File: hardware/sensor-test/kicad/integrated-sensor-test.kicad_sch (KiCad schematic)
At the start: 48 parts, among them J1 TYPE-C-31-M-12, J90 USB_B_Micro, J91 Conn_02x18_Odd_Even, J92 Conn_02x18_Odd_Even, J93 Conn_01x02, U1 RP2040, U10 USBLC6-2SC6, U2 W25Q128JVS, U3 AP2112K-3.3TRG1, U90 NCP1117-3.3_SOT223, Y1 ABLS-12.000MHZ-B4-T

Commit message: Mark retired Micro-USB data pins unconnected
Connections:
- net +1V1: no longer C11.1, C12.1, C13.1, U1.23 (DVDD), U1.45 (VREG_VOUT), U1.50 (DVDD)
- net +3V3: no longer C10.1, C16.1, C17.1, C3.1, C4.1, C5.1, C6.1, C7.1, C8.1, C9.1, C91.1, J91.2 (Pin_2), R8.1, U1.1 (IOVDD), U1.10 (IOVDD), U1.22 (IOVDD), U1.33 (IOVDD), U1.42 (IOVDD), U1.43 (ADC_AVDD), U1.44 (VREG_IN), U1.48 (USB_VDD), U1.49 (IOVDD), U2.8 (VCC), U90.2 (VO)
- net GND: no longer C10.2, C11.2, C12.2, C13.2, C15.2, C16.2, C3.2, C4.2, C5.2, C6.2, C7.2, C8.2, C9.2, J90.5 (GND), J90.6 (Shield), J91.1 (Pin_1), J91.11 (Pin_11), J91.13 (Pin_13), J91.15 (Pin_15), J91.17 (Pin_17), J91.19 (Pin_19), J91.21 (Pin_21), J91.23 (Pin_23), J91.25 (Pin_25), J91.27 (Pin_27), J91.29 (Pin_29), J91.3 (Pin_3), J91.31 (Pin_31), J91.33 (Pin_33), J91.35 (Pin_35), J91.36 (Pin_36), J91.5 (Pin_5), J91.7 (Pin_7), J91.9 (Pin_9), J92.10 (Pin_10), J92.12 (Pin_12), J92.14 (Pin_14), J92.16 (Pin_16), J92.18 (Pin_18), J92.2 (Pin_2), J92.20 (Pin_20), J92.22 (Pin_22), J92.24 (Pin_24), J92.26 (Pin_26), J92.28 (Pin_28), J92.30 (Pin_30), J92.32 (Pin_32), J92.34 (Pin_34), J92.35 (Pin_35), J92.36 (Pin_36), J92.4 (Pin_4), J92.6 (Pin_6), J92.8 (Pin_8), U1.19 (TESTEN), U1.57 (GND), U2.4 (GND)
- net GPIO0: no longer U1.2 (GPIO0)
- net GPIO1: no longer J91.6 (Pin_6)
- net GPIO10: no longer J91.24 (Pin_24), U1.13 (GPIO10)
- net GPIO11: no longer J91.26 (Pin_26), U1.14 (GPIO11)
- net GPIO12: no longer J91.28 (Pin_28)
- net GPIO13: no longer J91.30 (Pin_30)
- net GPIO14: no longer U1.17 (GPIO14)
- net GPIO15: no longer U1.18 (GPIO15)
- net GPIO16: no longer U1.27 (GPIO16)
- net GPIO17: no longer J92.25 (Pin_25), U1.28 (GPIO17)
- net GPIO18: no longer J92.23 (Pin_23)
- net GPIO19: no longer J92.21 (Pin_21), U1.30 (GPIO19)
- net GPIO2: no longer J91.8 (Pin_8), U1.4 (GPIO2)
- net GPIO20: no longer U1.31 (GPIO20)
- net GPIO21: no longer J92.17 (Pin_17)
- net GPIO22: no longer J92.15 (Pin_15), U1.34 (GPIO22)
- net GPIO23: no longer J92.13 (Pin_13), U1.35 (GPIO23)
- net GPIO24: no longer J92.11 (Pin_11), U1.36 (GPIO24)
- net GPIO25: no longer J92.9 (Pin_9), U1.37 (GPIO25)
- net GPIO26_ADC0: no longer U1.38 (GPIO26_ADC0)
- net GPIO27_ADC1: no longer J92.5 (Pin_5), U1.39 (GPIO27_ADC1)
- net GPIO28_ADC2: no longer J92.3 (Pin_3), U1.40 (GPIO28_ADC2)
- net GPIO29_ADC3: no longer J92.1 (Pin_1), U1.41 (GPIO29_ADC3)
- net GPIO3: no longer U1.5 (GPIO3)
- net GPIO4: no longer J91.12 (Pin_12), U1.6 (GPIO4)
- net GPIO5: no longer J91.14 (Pin_14), U1.7 (GPIO5)
- net GPIO6: no longer J91.16 (Pin_16)
- net GPIO7: no longer U1.9 (GPIO7)
- net GPIO8: no longer U1.11 (GPIO8)
- net GPIO9: no longer J91.22 (Pin_22), U1.12 (GPIO9)
- net QSPI_SCLK: no longer U1.52 (QSPI_SCLK), U2.6 (CLK)
- net QSPI_SD0: no longer U1.53 (QSPI_SD0)
- net QSPI_SD1: no longer U2.2 (DO(IO1))
- net QSPI_SD2: no longer U2.3 (IO2)
- net QSPI_SD3: no longer U1.51 (QSPI_SD3), U2.7 (IO3)
- net QSPI_SS: no longer R8.2, R9.1, U2.1 (~{CS})
- net RUN: no longer J92.29 (Pin_29), U1.26 (RUN)
- net SWCLK: no longer U1.24 (SWCLK)
- net SWD: no longer J92.31 (Pin_31), U1.25 (SWD)
- net VBUS: no longer C90.1, J90.1 (VBUS), U90.3 (VI)
- net XIN: no longer C15.1, U1.20 (XIN), Y1.1
- net XOUT: no longer R5.1, U1.21 (XOUT)
- net at U1.47 (USB_DP): no longer R3.2
- new net: C91.1, U90.2 (VO)
- now unconnected: C14.1, R5.2, Y1.2
- no-connect marks 4 -> 6

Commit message: Restore integrated wiring and retire Micro-USB data pins safely
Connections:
- net +1V1: now also C11.1, C12.1, C13.1, U1.23 (DVDD), U1.45 (VREG_VOUT), U1.50 (DVDD)
- net +3V3: now also C10.1, C16.1, C17.1, C3.1, C4.1, C5.1, C6.1, C7.1, C8.1, C9.1, C91.1, J91.2 (Pin_2), R8.1, U1.1 (IOVDD), U1.10 (IOVDD), U1.22 (IOVDD), U1.33 (IOVDD), U1.42 (IOVDD), U1.43 (ADC_AVDD), U1.44 (VREG_IN), U1.48 (USB_VDD), U1.49 (IOVDD), U2.8 (VCC), U90.2 (VO)
- net GND: now also C10.2, C11.2, C12.2, C13.2, C15.2, C16.2, C3.2, C4.2, C5.2, C6.2, C7.2, C8.2, C9.2, J90.5 (GND), J90.6 (Shield), J91.1 (Pin_1), J91.11 (Pin_11), J91.13 (Pin_13), J91.15 (Pin_15), J91.17 (Pin_17), J91.19 (Pin_19), J91.21 (Pin_21), J91.23 (Pin_23), J91.25 (Pin_25), J91.27 (Pin_27), J91.29 (Pin_29), J91.3 (Pin_3), J91.31 (Pin_31), J91.33 (Pin_33), J91.35 (Pin_35), J91.36 (Pin_36), J91.5 (Pin_5), J91.7 (Pin_7), J91.9 (Pin_9), J92.10 (Pin_10), J92.12 (Pin_12), J92.14 (Pin_14), J92.16 (Pin_16), J92.18 (Pin_18), J92.2 (Pin_2), J92.20 (Pin_20), J92.22 (Pin_22), J92.24 (Pin_24), J92.26 (Pin_26), J92.28 (Pin_28), J92.30 (Pin_30), J92.32 (Pin_32), J92.34 (Pin_34), J92.35 (Pin_35), J92.36 (Pin_36), J92.4 (Pin_4), J92.6 (Pin_6), J92.8 (Pin_8), U1.19 (TESTEN), U1.57 (GND), U2.4 (GND)
- net GPIO0: now also U1.2 (GPIO0)
- net GPIO1: now also J91.6 (Pin_6)
- net GPIO10: now also J91.24 (Pin_24), U1.13 (GPIO10)
- net GPIO11: now also J91.26 (Pin_26), U1.14 (GPIO11)
- net GPIO12: now also J91.28 (Pin_28)
- net GPIO13: now also J91.30 (Pin_30)
- net GPIO14: now also U1.17 (GPIO14)
- net GPIO15: now also U1.18 (GPIO15)
- net GPIO16: now also U1.27 (GPIO16)
- net GPIO17: now also J92.25 (Pin_25), U1.28 (GPIO17)
- net GPIO18: now also J92.23 (Pin_23)
- net GPIO19: now also J92.21 (Pin_21), U1.30 (GPIO19)
- net GPIO2: now also J91.8 (Pin_8), U1.4 (GPIO2)
- net GPIO20: now also U1.31 (GPIO20)
- net GPIO21: now also J92.17 (Pin_17)
- net GPIO22: now also J92.15 (Pin_15), U1.34 (GPIO22)
- net GPIO23: now also J92.13 (Pin_13), U1.35 (GPIO23)
- net GPIO24: now also J92.11 (Pin_11), U1.36 (GPIO24)
- net GPIO25: now also J92.9 (Pin_9), U1.37 (GPIO25)
- net GPIO26_ADC0: now also U1.38 (GPIO26_ADC0)
- net GPIO27_ADC1: now also J92.5 (Pin_5), U1.39 (GPIO27_ADC1)
- net GPIO28_ADC2: now also J92.3 (Pin_3), U1.40 (GPIO28_ADC2)
- net GPIO29_ADC3: now also J92.1 (Pin_1), U1.41 (GPIO29_ADC3)
- net GPIO3: now also U1.5 (GPIO3)
- net GPIO4: now also J91.12 (Pin_12), U1.6 (GPIO4)
- net GPIO5: now also J91.14 (Pin_14), U1.7 (GPIO5)
- net GPIO6: now also J91.16 (Pin_16)
- net GPIO7: now also U1.9 (GPIO7)
- net GPIO8: now also U1.11 (GPIO8)
- net GPIO9: now also J91.22 (Pin_22), U1.12 (GPIO9)
- net QSPI_SCLK: now also U1.52 (QSPI_SCLK), U2.6 (CLK)
- net QSPI_SD0: now also U1.53 (QSPI_SD0)
- net QSPI_SD1: now also U2.2 (DO(IO1))
- net QSPI_SD2: now also U2.3 (IO2)
- net QSPI_SD3: now also U1.51 (QSPI_SD3), U2.7 (IO3)
- net QSPI_SS: now also R8.2, R9.1, U2.1 (~{CS})
- net RUN: now also J92.29 (Pin_29), U1.26 (RUN)
- net SWCLK: now also U1.24 (SWCLK)
- net SWD: now also J92.31 (Pin_31), U1.25 (SWD)
- net VBUS: now also C90.1, J90.1 (VBUS), U90.3 (VI)
- net XIN: now also C15.1, U1.20 (XIN), Y1.1
- net XOUT: now also R5.1, U1.21 (XOUT)
- net at U1.47 (USB_DP): now also R3.2
- net at C14.1: now also R5.2, Y1.2

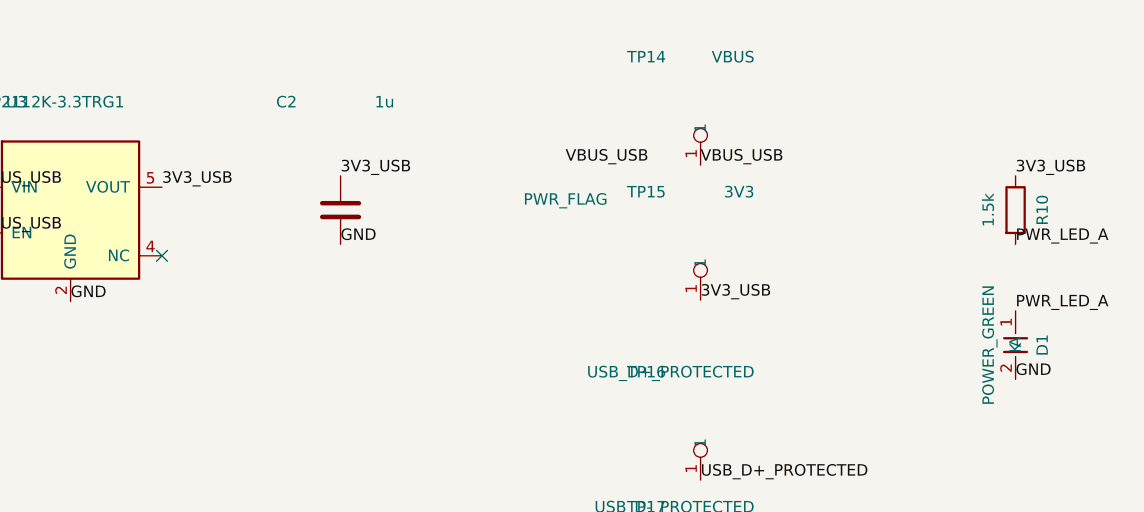
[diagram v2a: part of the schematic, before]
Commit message: Switch integrated 3V3 rail to AP2112
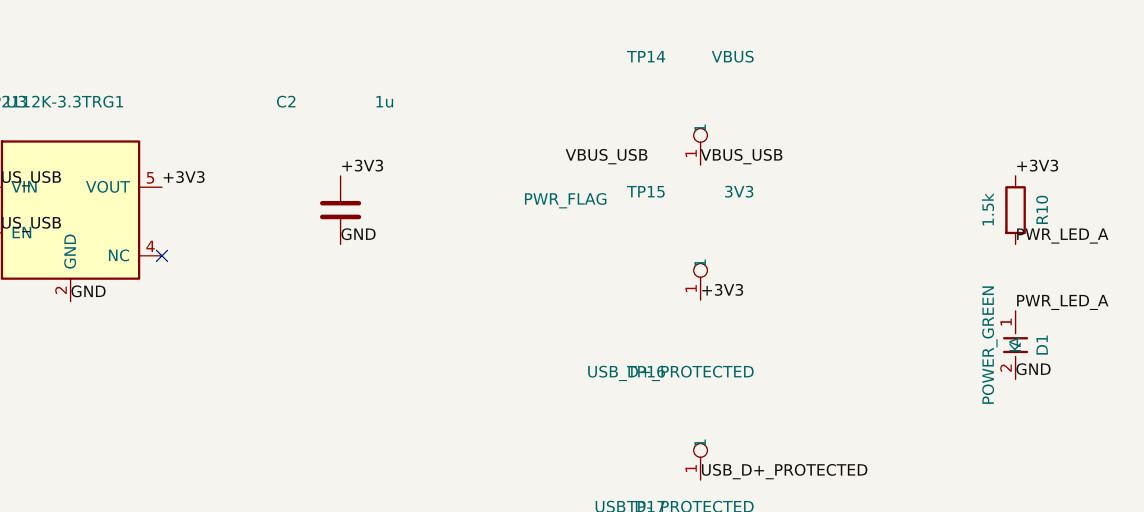
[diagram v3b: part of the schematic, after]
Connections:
- net 3V3_USB is gone; now on net +3V3: C2.1, R10.1, TP15.1, U3.5 (VOUT)
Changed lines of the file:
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@@
   (label "VBUS_USB" (at 454.84 47.46 0) (effects (font (size 1.27 1.27)) (justify left bottom)))
   (label "GND" (at 465 60.16 0) (effects (font (size 1.27 1.27)) (justify left bottom)))
-  (label "3V3_USB" (at 475.16 47.46 0) (effects (font (size 1.27 1.27)) (justify left bottom)))
+  (label "+3V3" (at 475.16 47.46 0) (effects (font (size 1.27 1.27)) (justify left bottom)))
   (label "VBUS_USB" (at 440 46.19 0) (effects (font (size 1.27 1.27)) (justify left bottom)))
   (label "GND" (at 440 53.81 0) (effects (font (size 1.27 1.27)) (justify left bottom)))
-  (label "3V3_USB" (at 495 46.19 0) (effects (font (size 1.27 1.27)) (justify left bottom)))
+  (label "+3V3" (at 495 46.19 0) (effects (font (size 1.27 1.27)) (justify left bottom)))
   (label "GND" (at 495 53.81 0) (effects (font (size 1.27 1.27)) (justify left bottom)))
   (symbol (lib_id "HEP:HRO_TYPE-C-31-M-12") (at 395 100 0) (unit 1)
@@
       )
     )
-  (label "3V3_USB" (at 535 60 0) (effects (font (size 1.27 1.27)) (justify left bottom)))
+  (label "+3V3" (at 535 60 0) (effects (font (size 1.27 1.27)) (justify left bottom)))
   (symbol (lib_id "Connector:TestPoint") (at 535 80 0) (unit 1)
       (in_bom no) (on_board yes) (dnp no)
@@
       (instances (project "integrated-sensor-test" (path "/0b572f4d-42c2-4e67-a259-3bf815f1855a" (reference "R10") (unit 1))))
     )
-  (label "3V3_USB" (at 570 46.19 0) (effects (font (size 1.27 1.27)) (justify left bottom)))
+  (label "+3V3" (at 570 46.19 0) (effects (font (size 1.27 1.27)) (justify left bottom)))
   (label "PWR_LED_A" (at 570 53.81 0) (effects (font (size 1.27 1.27)) (justify left bottom)))
   (symbol (lib_id "HEP:LED") (at 570 65 0) (unit 1)

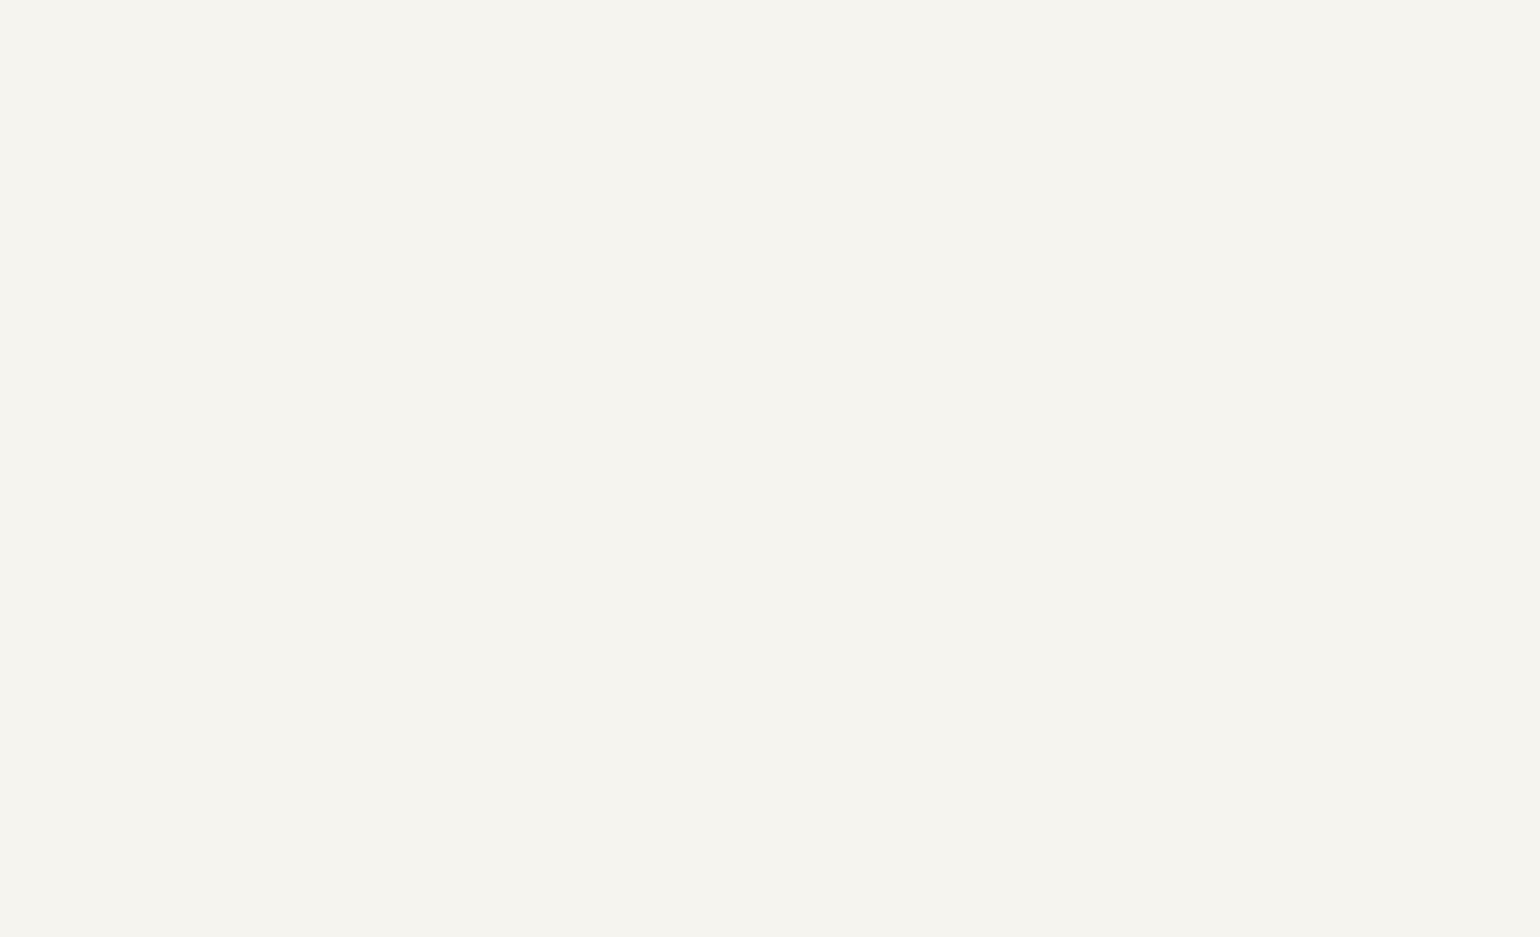
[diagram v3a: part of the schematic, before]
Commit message: Integrate Hall acquisition block
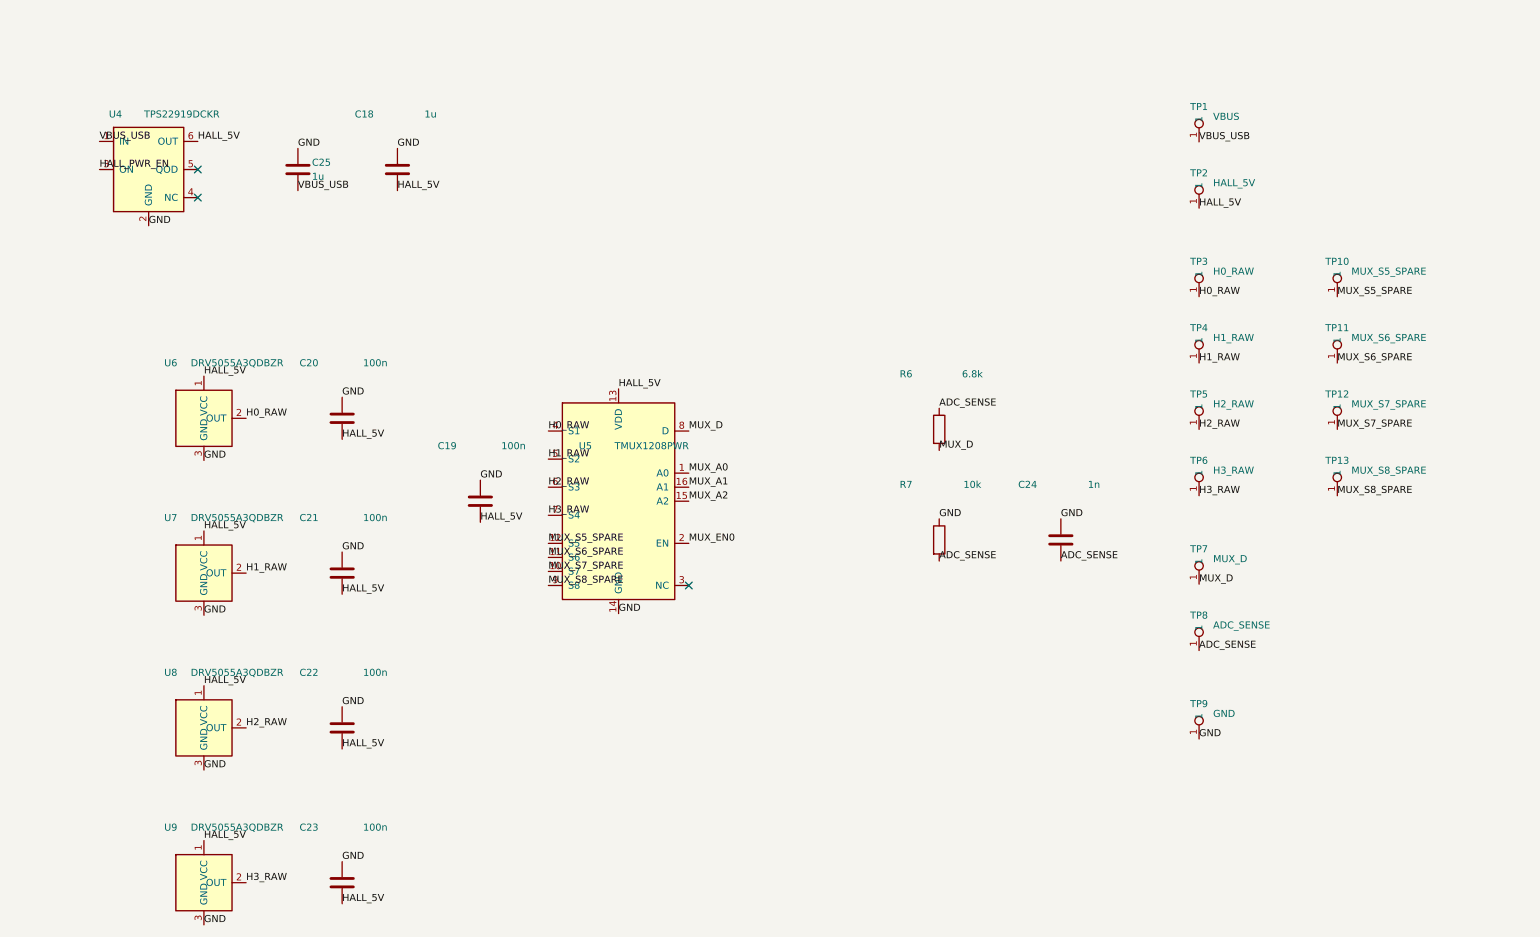
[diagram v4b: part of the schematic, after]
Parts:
- added C18, C25: 1u, Capacitor_SMD:C_0603_1608Metric, symbol Device:C
- added C19, C20, C21, C22, C23: 100n, Capacitor_SMD:C_0603_1608Metric, symbol Device:C
- added C24: 1n, Capacitor_SMD:C_0603_1608Metric, symbol Device:C
- added R6: 6.8k, Resistor_SMD:R_0603_1608Metric, symbol Device:R
- added R7: 10k, Resistor_SMD:R_0603_1608Metric, symbol Device:R
- added TP1: VBUS, TestPoint:TestPoint_Pad_D1.5mm, symbol Connector:TestPoint
- added TP10: MUX_S5_SPARE, TestPoint:TestPoint_Pad_D1.5mm, symbol Connector:TestPoint
- added TP11: MUX_S6_SPARE, TestPoint:TestPoint_Pad_D1.5mm, symbol Connector:TestPoint
- added TP12: MUX_S7_SPARE, TestPoint:TestPoint_Pad_D1.5mm, symbol Connector:TestPoint
- added TP13: MUX_S8_SPARE, TestPoint:TestPoint_Pad_D1.5mm, symbol Connector:TestPoint
- added TP2: HALL_5V, TestPoint:TestPoint_Pad_D1.5mm, symbol Connector:TestPoint
- added TP3: H0_RAW, TestPoint:TestPoint_Pad_D1.5mm, symbol Connector:TestPoint
- added TP4: H1_RAW, TestPoint:TestPoint_Pad_D1.5mm, symbol Connector:TestPoint
- added TP5: H2_RAW, TestPoint:TestPoint_Pad_D1.5mm, symbol Connector:TestPoint
- added TP6: H3_RAW, TestPoint:TestPoint_Pad_D1.5mm, symbol Connector:TestPoint
- added TP7: MUX_D, TestPoint:TestPoint_Pad_D1.5mm, symbol Connector:TestPoint
- added TP8: ADC_SENSE, TestPoint:TestPoint_Pad_D1.5mm, symbol Connector:TestPoint
- added TP9: GND, TestPoint:TestPoint_Pad_D1.5mm, symbol Connector:TestPoint
- added U4: TPS22919DCKR, Package_TO_SOT_SMD:SOT-363_SC-70-6, symbol HEP:TPS22919DCKR
- added U5: TMUX1208PWR, Package_SO:TSSOP-16_4.4x5mm_P0.65mm, symbol HEP:TMUX1208PWR
- added U6, U7, U8, U9: DRV5055A3QDBZR, marbastlib-he:SW_MX_HE_0deg_1u, symbol HEP:DRV5055A3QDBZR
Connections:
- net GND: now also C18.1, C19.1, C20.1, C21.1, C22.1, C23.1, C24.1, C25.1, R7.1, TP9.1, U4.2 (GND), U5.14 (GND), U6.3 (GND), U7.3 (GND), U8.3 (GND), U9.3 (GND)
- net VBUS_USB: now also C25.2, TP1.1, U4.1 (IN)
- new net ADC_SENSE: C24.2, R6.1, R7.2, TP8.1
- new net H0_RAW: TP3.1, U5.4 (S1), U6.2 (OUT)
- new net H1_RAW: TP4.1, U5.5 (S2), U7.2 (OUT)
- new net H2_RAW: TP5.1, U5.6 (S3), U8.2 (OUT)
- new net H3_RAW: TP6.1, U5.7 (S4), U9.2 (OUT)
- new net HALL_5V: C18.2, C19.2, C20.2, C21.2, C22.2, C23.2, TP2.1, U4.6 (OUT), U5.13 (VDD), U6.1 (VCC), U7.1 (VCC), U8.1 (VCC), U9.1 (VCC)
- new net HALL_PWR_EN: U4.3 (ON)
- new net MUX_A0: U5.1 (A0)
- new net MUX_A1: U5.16 (A1)
- new net MUX_A2: U5.15 (A2)
- new net MUX_D: R6.2, TP7.1, U5.8 (D)
- new net MUX_EN0: U5.2 (EN)
- new net MUX_S5_SPARE: TP10.1, U5.12 (S5)
- new net MUX_S6_SPARE: TP11.1, U5.11 (S6)
- new net MUX_S7_SPARE: TP12.1, U5.10 (S7)
- new net MUX_S8_SPARE: TP13.1, U5.9 (S8)
- no-connect marks 6 -> 9

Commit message: Connect Hall controls and sync evidence dashboard
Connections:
- net GPIO2: no longer U1.4 (GPIO2)
- net GPIO3: no longer U1.5 (GPIO3)
- net GPIO4: no longer U1.6 (GPIO4)
- net GPIO5: no longer U1.7 (GPIO5)
- net GPIO7: no longer U1.9 (GPIO7)
- net HALL_PWR_EN: now also U1.9 (GPIO7)
- net MUX_A0: now also U1.4 (GPIO2)
- net MUX_A1: now also U1.5 (GPIO3)
- net MUX_A2: now also U1.6 (GPIO4)
- net MUX_EN0: now also U1.7 (GPIO5)
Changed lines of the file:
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@@
     (effects (font (size 1.27 1.27)) (justify right bottom))
   )
-  (label "GPIO5" (at 245.11 124.46 180) (fields_autoplaced)
+  (label "MUX_EN0" (at 245.11 124.46 180) (fields_autoplaced)
     (effects (font (size 1.27 1.27)) (justify right bottom))
   )
@@
     (effects (font (size 1.27 1.27)) (justify right bottom))
   )
-  (label "GPIO4" (at 245.11 121.92 180) (fields_autoplaced)
+  (label "MUX_A2" (at 245.11 121.92 180) (fields_autoplaced)
     (effects (font (size 1.27 1.27)) (justify right bottom))
   )
@@
     (effects (font (size 1.27 1.27)) (justify right bottom))
   )
-  (label "GPIO2" (at 245.11 116.84 180) (fields_autoplaced)
+  (label "MUX_A0" (at 245.11 116.84 180) (fields_autoplaced)
     (effects (font (size 1.27 1.27)) (justify right bottom))
   )
@@
     (effects (font (size 1.27 1.27)) (justify left bottom))
   )
-  (label "GPIO7" (at 245.11 129.54 180) (fields_autoplaced)
+  (label "HALL_PWR_EN" (at 245.11 129.54 180) (fields_autoplaced)
     (effects (font (size 1.27 1.27)) (justify right bottom))
   )
@@
     (effects (font (size 1.27 1.27)) (justify left bottom))
   )
-  (label "GPIO3" (at 245.11 119.38 180) (fields_autoplaced)
+  (label "MUX_A1" (at 245.11 119.38 180) (fields_autoplaced)
     (effects (font (size 1.27 1.27)) (justify right bottom))
   )
